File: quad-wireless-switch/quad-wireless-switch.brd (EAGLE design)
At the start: 38.1 x 108 mm, 69 parts, among them IC1 LM2937IMP-3.3, Q1 DN2625K4-G, Q2 SI2323DS-T1-E3, Q3 IRL520, Q4 IRL520, Q5 IRL520, Q6 IRL520, U1 ATMEGA328P_TQFP

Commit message: quad wireless switch wip
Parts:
- added D3, D4, D5, D6: 1N4004, diode:DO41-10
- added OK1, OK2, OK3, OK4: 4N35SM, optocoupler:DIL6-SMD
- added R24, R28, R29: 220, microbuilder:0805
- added R25, R26, R30, R31: 10K, microbuilder:0805
- added R27: 150, microbuilder:0805
- R10, R16: value 10k -> 10K
- R11: value 10k -> 150
- R13, R20, R21, R22: value 150 -> 220
- R14: value 10k -> 220
- R15, R23: value 150 -> 10K
- moved R23 189.5 mm to (1.02, -95.2), flipped to the top
- moved R17 182.4 mm to (6.35, -88.4), flipped to the top, turned to 0 degrees
- moved R22 178.0 mm to (-5.33, -95.2), flipped to the top
- moved LED3 175.9 mm to (-3.81, -90.7)
- moved Q5 167.4 mm to (-2.03, -83.3), turned to 0 degrees
- moved R16 161.5 mm to (1.02, -63.0), flipped to the top, turned to 0 degrees
- moved R21 156.4 mm to (12.7, -88.4), flipped to the top
- moved R15 145.6 mm to (-5.33, -63.0), flipped to the top, turned to 0 degrees
- moved R14 141.5 mm to (12.7, -56.1), flipped to the top, turned to 0 degrees
- moved R11 135.8 mm to (7.37, -63.0), flipped to the top, turned to 0 degrees
- moved LED2 131.8 mm to (-3.81, -58.4)
- moved R13 124.8 mm to (6.35, -56.1), flipped to the top, turned to 0 degrees
- moved Q4 123.0 mm to (-2.03, -51.1), turned to 0 degrees
- moved R10 92.7 mm to (-5.33, -30.7), flipped to the top, turned to 0 degrees
- moved OUT1 12.7 mm to (33.3, 44.5)
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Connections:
- removed net OUT2_GATE: Q4.1, R13.2
- removed net OUT3_GATE: Q5.1, R15.2
- removed net OUT4_GATE: Q6.1, R17.2
- new net N$21: OK1.5, R25.1
- new net N$23: OK1.1, R24.1
- new net N$24: D5.A, OUT3.1, Q5.2
- new net N$25: LED3.K, R21.1
- new net N$26: OK3.5, R23.1
- new net N$27: OK3.1, R22.1
- new net N$28: OK3.4, R17.1, R26.2
- new net N$29: D6.A, OUT4.1, Q6.2
- new net N$30: LED4.K, R28.1
- new net N$31: OK4.5, R30.1
- new net N$32: OK4.1, R29.1
- new net N$33: OK4.4, R27.1, R31.2
- net 12V: now also D3.C, D4.C, D5.C, D6.C, R15.2, R23.2, R25.2, R30.2
- net GND: now also OK1.2, OK2.2, OK3.2, OK4.2, R10.1, R13.2, R16.1, R26.1, R28.2, R31.1; no longer R10.2, R11.2, R14.2, R16.2, R22.2, R23.2
- net N$18: now also OK2.1, R14.1; no longer OUT3.1, Q5.2
- net N$2: now also OK1.4, R10.2, R12.1; no longer LED2.K, R21.1
- net N$22: now also OK2.4, R11.1, R16.2; no longer OUT4.1, Q6.2
- net N$3: now also D4.A, OUT2.1, Q4.2; no longer LED3.K, R22.1
- net N$4: now also LED2.K, R13.1; no longer LED4.K, R23.1
- net N$6: now also D3.A
- net N$8: now also OK2.5, R15.1; no longer OUT2.1, Q4.2
- net OUT1: now also R24.2; no longer R10.1, R12.1
- net OUT1_GATE: now also Q4.1, Q5.1, Q6.1, R11.2, R17.2, R27.2
- net OUT2: now also R14.2; no longer R11.1, R13.1
- net OUT3: now also R22.2; no longer R14.1, R15.1
- net OUT4: now also R29.2; no longer R16.1, R17.1
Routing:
- net 12V: track 116.8 -> 101.1 mm
- net N$22: track 15.6 -> 0.00 mm
- net N$18: track 15.6 -> 0.00 mm
- net N$8: track 15.6 -> 0.00 mm
- net N$6: track 15.6 -> 0.00 mm
- net OUT4: track 64.2 -> 48.9 mm
- net OUT3: track 50.9 -> 36.3 mm
- net OUT2: track 46.6 -> 32.2 mm
- net OUT1: track 31.5 -> 19.1 mm
- net OUT1_GATE: track 5.16 -> 0.27 mm
- net OUT4_GATE: track 4.85 -> 0.00 mm
- net OUT2_GATE: track 4.85 -> 0.00 mm
- net OUT3_GATE: track 4.85 -> 0.00 mm
- net N$4: track 2.82 -> 0.00 mm
- net N$3: track 2.82 -> 0.00 mm
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
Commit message: wip
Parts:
- R1: value 10k -> 100k
- R10, R23, R25: value 10K -> 220
- R11, R12: value 150 -> 10k
- R14, R28, R29: value 220 -> 10K
- R17, R27: value 150 -> 10K
- R18, R19: value 10k -> 150
- R2: value 10k -> 39k
- R20, R21: value 220 -> 10k
- R3: value 100k -> 10k
- R30, R31: value 10K -> 150
- R4: value 39k -> 220
- R7: value 10k -> 220
- moved R26 200.9 mm to (8.38, 105.7), flipped to the bottom, turned to 270 degrees
- moved R22 191.2 mm to (23.9, 93.7), flipped to the bottom, turned to 270 degrees
- moved Q5 188.7 mm to (25.7, 103.4)
- moved D5 179.9 mm to (23.9, 97.8), turned to 180 degrees
- moved R23 179.0 mm to (13.2, 83.3), flipped to the bottom, turned to 270 degrees
- moved R21 177.9 mm to (8.38, 89.4), flipped to the bottom, turned to 90 degrees
- moved OK3 172.0 mm to (14.2, 102.1), flipped to the bottom
- moved LED3 171.8 mm to (27.4, 78.2)
- moved R17 150.2 mm to (24.1, 60.7), flipped to the bottom, turned to 90 degrees
- moved R15 143.7 mm to (21.3, 78.2), flipped to the bottom, turned to 180 degrees
- moved R14 134.9 mm to (13.5, 78.7), flipped to the bottom, turned to 270 degrees
- moved LED2 122.7 mm to (27.7, 60.2)
- moved R16 119.9 mm to (26.7, 54.1), flipped to the bottom, turned to 270 degrees
- moved R11 118.4 mm to (8.64, 55.4), flipped to the bottom, turned to 90 degrees
- moved R24 112.9 mm to (27.7, 91.7), flipped to the bottom
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- renumbered IN to X1, IN1 to X2, IN2 to X3, IN3 to X4, IN4 to X6, ISP to J1, NRF to JP1, SER to JP2
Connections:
- removed net N$32 (its old number): OK4.1, R29.1
- new net N$27: OK4.1, R23.1
- new net OUT2_GATE: Q3.1, R18.2
- new net OUT3_GATE: Q6.1, R31.2
- new net OUT4_GATE: Q5.1, R30.2
- net 12V: now also R1.2, R17.2, R27.2, R29.2; no longer R23.2, R25.2, R3.2, R30.2
- net 3.3V: now also R11.1, R12.1, R20.1, R21.1, R3.2; no longer R1.1, R18.1, R19.1, R2.1, R7.2
- net CSN: now also R5.1; no longer R7.1
- net GND: now also R10.2, R14.1, R2.2, R24.2, R25.2, R28.1; no longer R10.1, R20.2, R21.2, R28.2, R31.1, R4.2
- net IN1: now also R11.2; no longer R1.2
- net IN2: now also R12.2; no longer R2.2
- net IN3: now also R20.2; no longer R18.2
- net IN4: now also R21.2; no longer R19.2
- net MISO: now also R6.1; no longer R8.1
- net MOSI: now also R4.2; no longer R6.2
- net N$1: now also R13.1; no longer R20.1
- net N$11: now also R1.1; no longer R3.1
- net N$14: now also R2.1; no longer R4.1
- net N$18: now also OK1.1, R8.1; no longer OK2.1, R14.1
- net N$2: now also OK2.4, R16.2, R19.1; no longer OK1.4, R10.2, R12.1
- net N$21: now also OK2.5, R17.1; no longer OK1.5, R25.1
- net N$22: now also OK1.4, R14.2, R18.1; no longer OK2.4, R11.1, R16.2
- net N$23: now also OK2.1, R9.1; no longer OK1.1, R24.1
- net N$24: now also D6.A, Q6.2; no longer D5.A, Q5.2
- net N$25: now also R25.1; no longer R21.1
- net N$26: now also OK4.5, R29.1; no longer OK3.5, R23.1
- net N$28: now also OK4.4, R28.2, R31.1; no longer OK3.4, R17.1, R26.2
- net N$29: now also D5.A, Q5.2; no longer D6.A, Q6.2
- net N$3: now also D3.A, Q3.2; no longer D4.A, Q4.2
- net N$30: now also R24.1; no longer R28.1
- net N$31: now also OK3.5, R27.1; no longer OK4.5, R30.1
- net N$33: now also OK3.4, R26.2, R30.1; no longer OK4.4, R27.1, R31.2
- net N$4: now also R10.1; no longer R13.1
- net N$6: now also D4.A, Q4.2; no longer D3.A, Q3.2
- net N$66: now also R7.2; no longer R9.2
- net N$7: now also R4.1; no longer R6.1
- net N$8: now also OK1.5; no longer OK2.5
- net N$9: now also R6.2; no longer R8.2
- net OUT1: now also R9.2; no longer R24.2
- net OUT1_GATE: now also R19.2; no longer Q3.1, Q5.1, Q6.1, R11.2, R12.2, R17.2, R27.2
- net OUT2: now also R8.2; no longer R14.2
- net OUT3: now also R23.2; no longer R22.2
- net OUT4: now also R22.2; no longer R29.2
- net RESET: now also R3.1; no longer R5.1
- net SCK: now also R7.1; no longer R9.1
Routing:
- net 12V: track 101.1 -> 167.2 mm, vias 0 -> 3
- net N$29: track 0.00 -> 31.1 mm
- net N$6: track 0.00 -> 30.2 mm
- net N$3: track 0.00 -> 28.6 mm
- net N$24: track 0.00 -> 28.6 mm
- net OUT3_GATE: track 0.00 -> 19.7 mm
- net OUT2_GATE: track 0.00 -> 19.2 mm
- net N$31: track 0.00 -> 18.7 mm
- net OUT3: track 36.3 -> 52.6 mm
- net OUT4_GATE: track 0.00 -> 16.0 mm
- net N$32: track 0.00 -> 13.8 mm
- net N$2: track 0.00 -> 13.7 mm
- net OUT4: track 48.9 -> 58.9 mm, vias 0 -> 1
- net N$28: track 0.00 -> 9.41 mm
- net OUT2: track 32.2 -> 41.0 mm
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
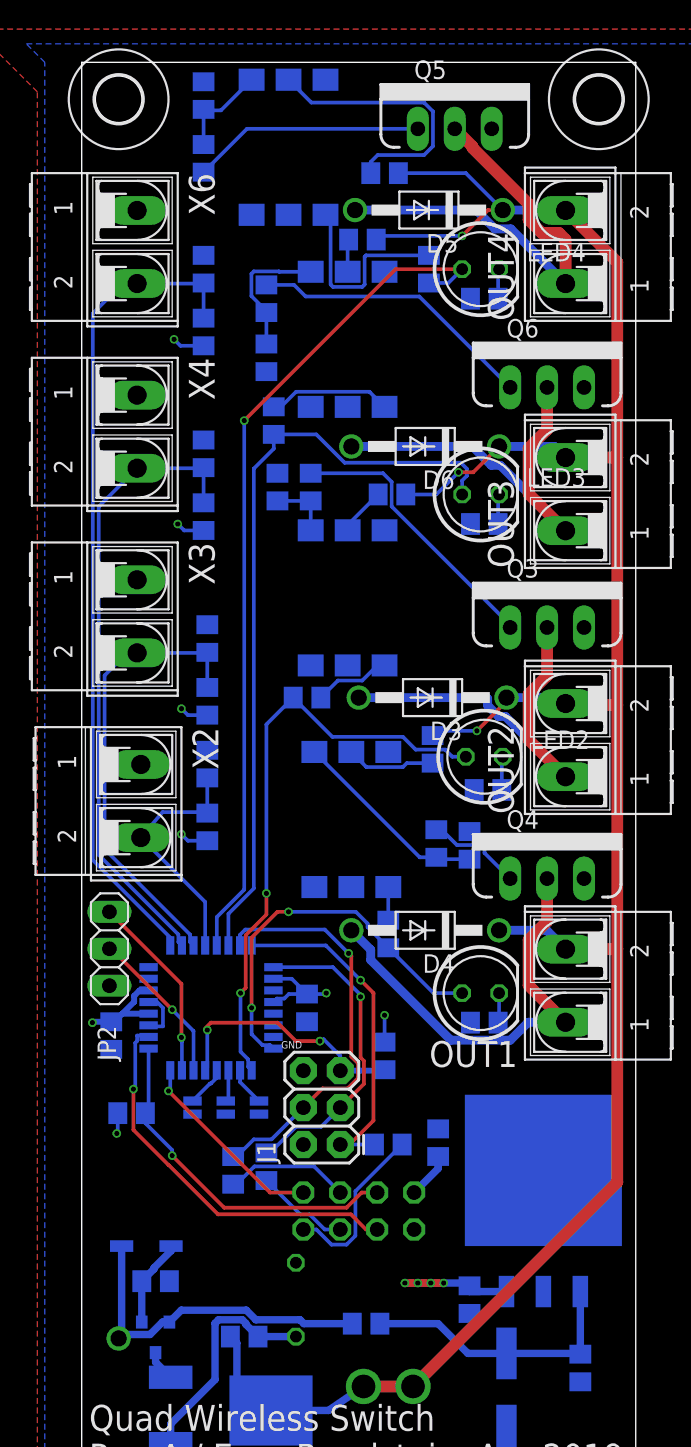
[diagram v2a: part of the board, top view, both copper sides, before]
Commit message: quad wireless switch with nrf24
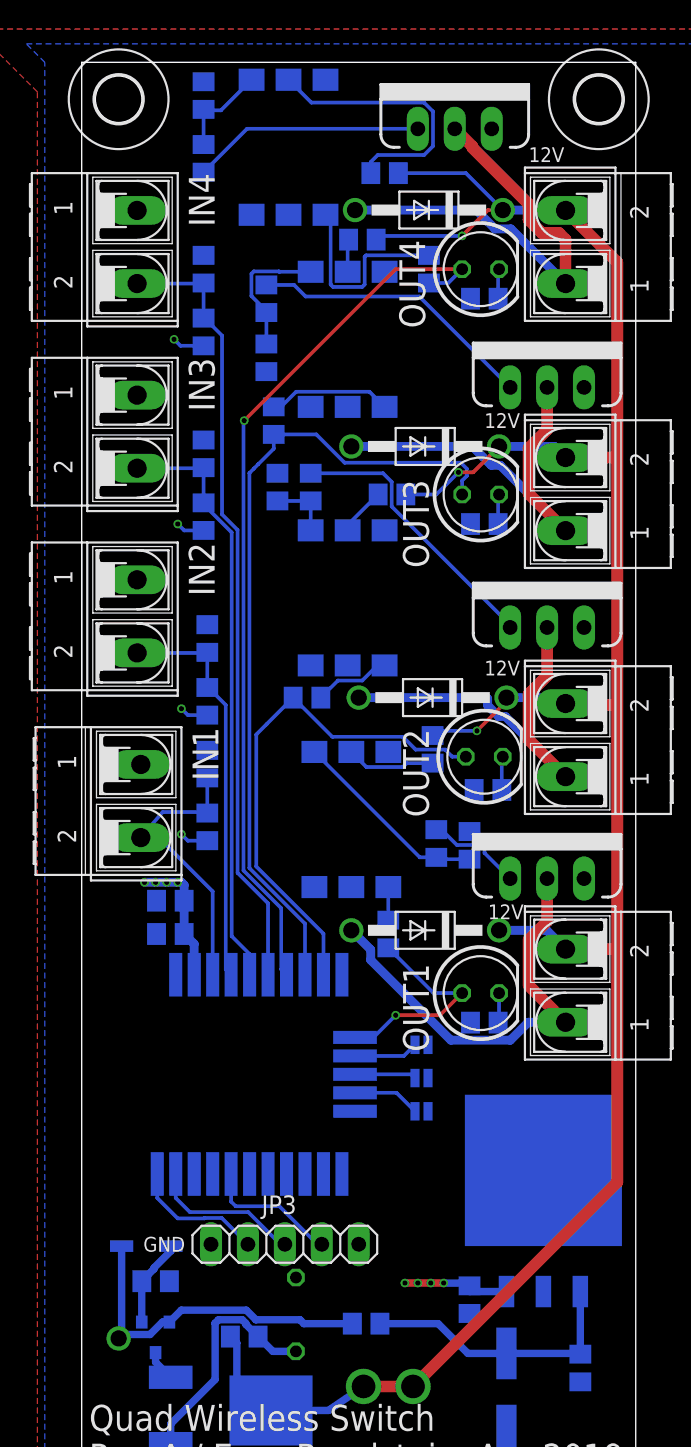
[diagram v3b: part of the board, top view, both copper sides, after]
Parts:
- removed C1, C2: 0.1uF, microbuilder:0805
- removed C3: 4.7uF, microbuilder:0805
- removed J1: AVR_SPI_PRG_6PTH, SparkFun-Connectors:2X3
- removed JP1: (no value), pinhead:2X04
- removed JP2: (no value), pinhead:1X03
- removed R3, R5: 10k, microbuilder:0805
- removed R4, R6, R7: 220, microbuilder:0805
- removed SJ1, SJ2, SJ3: SOLDERJUMPERNO, SparkFun-Retired:SJ_2S-NO
- removed U1: ATMEGA328P_TQFP, SparkFun-DigitalIC:TQFP32-08
- added C11: 0.1uF, microbuilder:0805
- added C12: 10uF, microbuilder:0805
- added JP3: (no value), pinhead:1X05
- added SJ4, SJ5, SJ6: SOLDERJUMPERNO, SparkFun-Retired:SJ_2S-NO
- added U2: SDB501, shlomo:SKB501
- moved D1 1.02 mm to (14.7, 21.8)
- renumbered X2 to IN1, X3 to IN2, X4 to IN3, X6 to IN4
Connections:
- removed net CE: JP1.3, U1.2
- removed net CSN: JP1.4, R5.1, U1.1
- removed net IRQ: JP1.8, U1.32
- removed net MISO: J1.1, R6.1, U1.16
- removed net MOSI: J1.4, R4.2, U1.15
- removed net N$12: SJ2.1, U1.27
- removed net N$16: SJ3.1, U1.28
- removed net N$19: JP2.3, U1.31
- removed net N$20: JP2.2, U1.30
- removed net N$66: JP1.5, R7.2
- removed net RESET: J1.5, R3.1, U1.29
- removed net SCK: J1.3, R7.1, U1.17
- new net N$36: JP3.2, U2.26
- new net N$37: JP3.3, U2.25
- new net N$38: JP3.4, U2.22
- net 3.3V: now also C11.1, C12.1, JP3.5, U2.2; no longer C1.2, C2.2, C3.2, J1.2, JP1.2, R3.2, R5.2, U1.18, U1.20, U1.4, U1.6
- net GND: now also C11.2, C12.2, JP3.1, SJ4.1, SJ5.1, SJ6.1, U2.1, U2.10; no longer C1.1, C2.1, C3.1, J1.6, JP1.1, JP2.1, SJ1.2, SJ2.2, SJ3.2, U1.21, U1.3, U1.5
- net IN1: now also U2.3; no longer U1.12
- net IN2: now also U2.4; no longer U1.11
- net IN3: now also U2.5; no longer U1.10
- net IN4: now also U2.6; no longer U1.9
- net N$10: now also SJ6.2, U2.12; no longer SJ1.1, U1.26
- net N$7: now also SJ4.2, U2.14; no longer JP1.6, R4.1
- net N$9: now also SJ5.2, U2.13; no longer JP1.7, R6.2
- net OUT1: now also U2.11; no longer U1.24
- net OUT2: now also U2.9; no longer U1.25
- net OUT3: now also U2.8; no longer U1.14
- net OUT4: now also U2.7; no longer U1.13
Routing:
- net MOSI: track 28.7 -> 0.00 mm, vias 1 -> 0
- net CE: track 27.0 -> 0.00 mm, vias 1 -> 0
- net CSN: track 24.2 -> 0.00 mm, vias 1 -> 0
- net MISO: track 23.8 -> 0.00 mm, vias 1 -> 0
- net SCK: track 21.7 -> 0.00 mm, vias 1 -> 0
- net RESET: track 17.6 -> 0.00 mm, vias 2 -> 0
- net IRQ: track 13.6 -> 0.00 mm, vias 1 -> 0
- net N$19: track 13.0 -> 0.00 mm, vias 1 -> 0
- net OUT1: track 26.2 -> 15.0 mm, vias 2 -> 1
- net N$20: track 10.8 -> 0.00 mm, vias 1 -> 0
- net 3.3V: track 38.2 -> 27.6 mm
- net N$37: track 0.00 -> 10.5 mm
- net N$38: track 0.00 -> 9.35 mm
- net N$36: track 0.00 -> 9.22 mm
- net N$9: track 11.9 -> 4.23 mm
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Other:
- board text added: "Eran Rundstein, 2019"
- board text added: "Quad Wireless Switch"
- board text removed: "IRQ"

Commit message: wip
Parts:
- added JP1: (no value), pinhead:1X02
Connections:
- net 3.3V: now also JP1.2
- net GND: now also JP1.1
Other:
- board text added: "3.3v"
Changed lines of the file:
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@@
 <wire x1="38.1" y1="107.95" x2="0" y2="107.95" width="0" layer="20"/>
 <wire x1="0" y1="107.95" x2="0" y2="0" width="0" layer="20"/>
-<text x="0.508" y="11.176" size="1.778" layer="25">Quad Wireless Switch
+<text x="0.508" y="11.176" size="1.524" layer="25">Quad Wireless Switch
 Rev A / Eran Rundstein, Apr 2019</text>
 <text x="13.208" y="6.604" size="0.889" layer="25">+12V</text>
@@
 <text x="27.686" y="65.786" size="1.016" layer="21">12V</text>
 <text x="27.94" y="49.022" size="1.016" layer="21">12V</text>
+<text x="29.972" y="1.524" size="1.016" layer="21" rot="R90">3.3v</text>
+<text x="27.686" y="1.27" size="1.016" layer="21" rot="R90">GND</text>
 </plain>
 <attributes>
@@
 <attribute name="NAME" x="25.292" y="40.132" size="0.4064" layer="26" rot="MR0"/>
 </element>
+<element name="JP1" library="pinhead" library_urn="urn:adsk.eagle:library:325" package="1X02" package3d_urn="urn:adsk.eagle:package:22435/2" value="" x="28.702" y="6.096" smashed="yes">
+<attribute name="NAME" x="26.0858" y="7.9248" size="1.27" layer="25" ratio="10"/>
+<attribute name="VALUE" x="26.162" y="2.921" size="1.27" layer="27"/>
+</element>
 </elements>
 <signals>
@@
 <contactref element="C11" pad="2"/>
 <contactref element="C12" pad="2"/>
+<contactref element="JP1" pad="1"/>
 </signal>
 <signal name="3.3V">
@@
 <via x="5.842" y="51.562" extent="1-16" drill="0.35"/>
 <via x="6.604" y="51.562" extent="1-16" drill="0.35"/>
+<contactref element="JP1" pad="2"/>
 </signal>
 <signal name="N$11">
